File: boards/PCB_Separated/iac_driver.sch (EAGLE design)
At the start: 8 parts, among them IC1 L293D

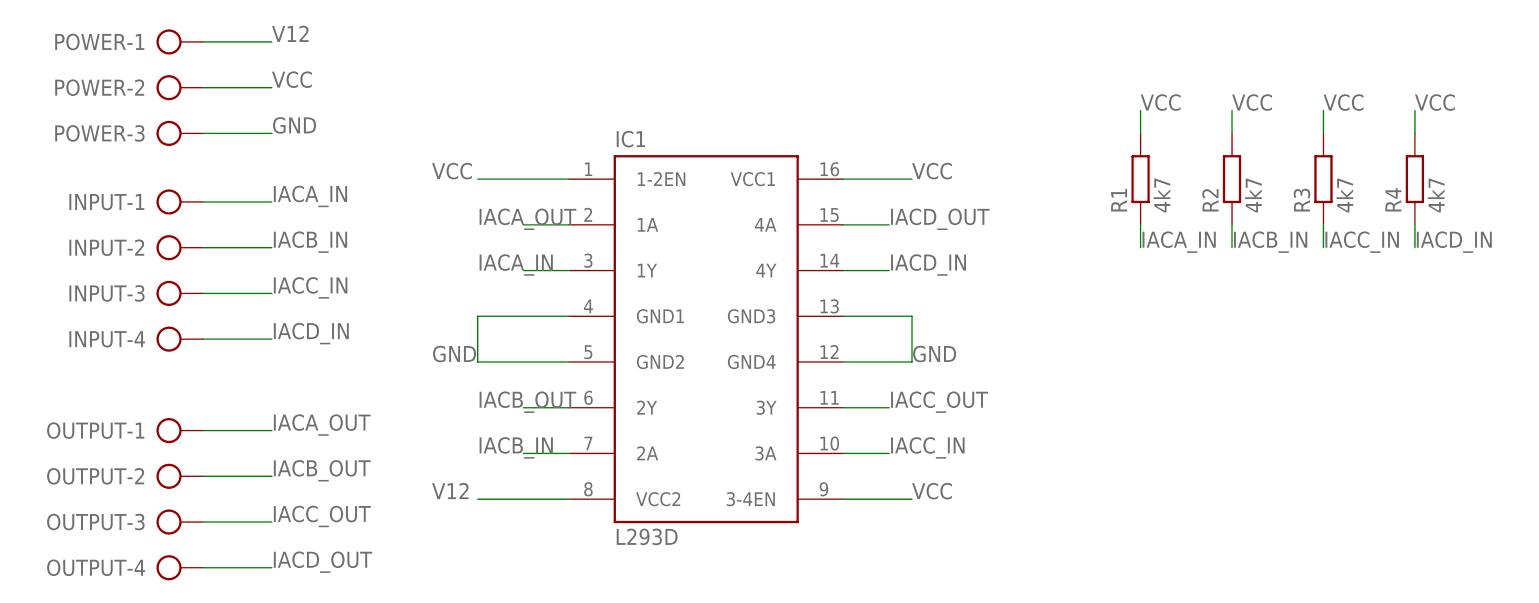
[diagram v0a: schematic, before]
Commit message: IAC progress. Valve already driven, but there a problem with voltage while USB connected to PC
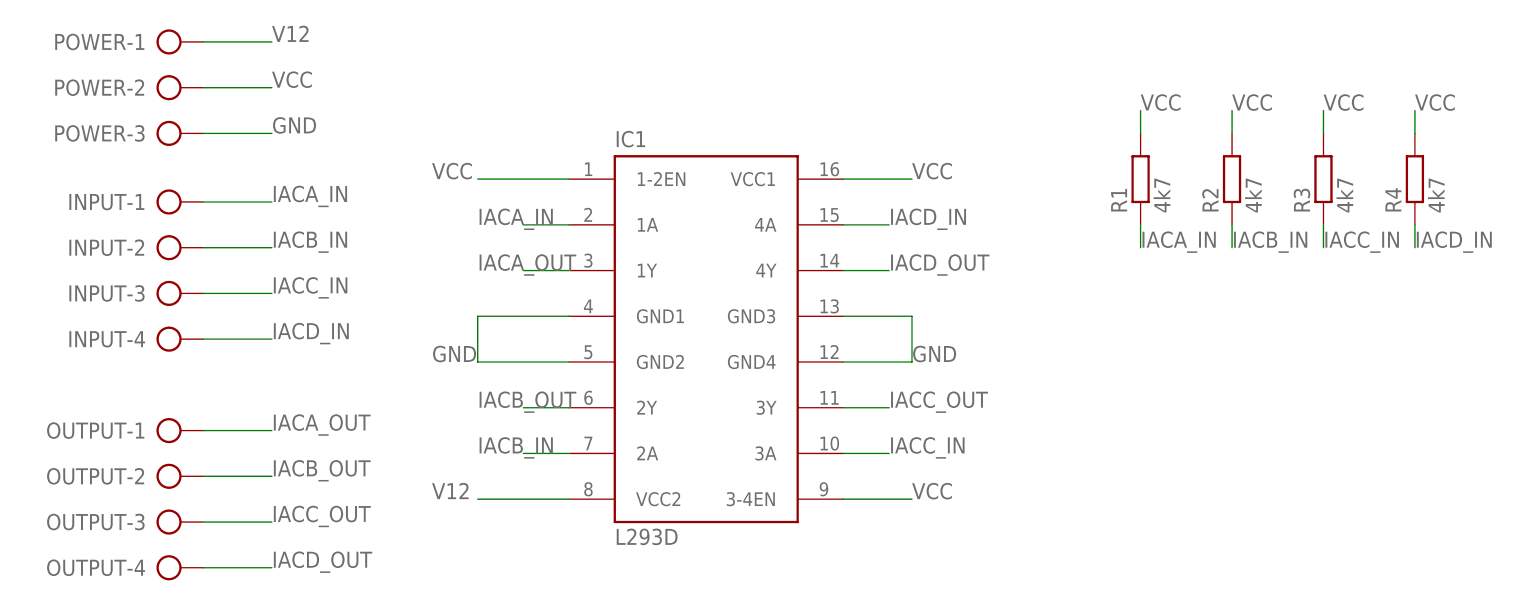
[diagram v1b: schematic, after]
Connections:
- net IACA_IN: now also IC1.1A; no longer IC1.1Y
- net IACA_OUT: now also IC1.1Y; no longer IC1.1A
- net IACD_IN: now also IC1.4A; no longer IC1.4Y
- net IACD_OUT: now also IC1.4Y; no longer IC1.4A
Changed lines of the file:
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@@
 <net name="IACA_OUT" class="0">
-<segment>
-<pinref part="IC1" gate="G$1" pin="1A"/>
-<wire x1="45.72" y1="35.56" x2="40.64" y2="35.56" width="0.1524" layer="91"/>
-<label x="35.56" y="35.56" size="1.778" layer="95"/>
-</segment>
 <segment>
 <pinref part="OUTPUT" gate="-1" pin="KL"/>
@@
 <label x="12.7" y="12.7" size="1.778" layer="95"/>
 </segment>
-</net>
-<net name="IACA_IN" class="0">
 <segment>
 <pinref part="IC1" gate="G$1" pin="1Y"/>
@@
 <label x="35.56" y="30.48" size="1.778" layer="95"/>
 </segment>
+</net>
+<net name="IACA_IN" class="0">
 <segment>
 <pinref part="R1" gate="G$1" pin="1"/>
@@
 <wire x1="5.08" y1="38.1" x2="12.7" y2="38.1" width="0.1524" layer="91"/>
 <label x="12.7" y="38.1" size="1.778" layer="95"/>
+</segment>
+<segment>
+<pinref part="IC1" gate="G$1" pin="1A"/>
+<wire x1="45.72" y1="35.56" x2="40.64" y2="35.56" width="0.1524" layer="91"/>
+<label x="35.56" y="35.56" size="1.778" layer="95"/>
 </segment>
 </net>
@@
 <net name="IACD_OUT" class="0">
 <segment>
-<pinref part="IC1" gate="G$1" pin="4A"/>
-<wire x1="76.2" y1="35.56" x2="81.28" y2="35.56" width="0.1524" layer="91"/>
-<label x="81.28" y="35.56" size="1.778" layer="95"/>
-</segment>
-<segment>
 <pinref part="OUTPUT" gate="-4" pin="KL"/>
 <wire x1="5.08" y1="-2.54" x2="12.7" y2="-2.54" width="0.1524" layer="91"/>
 <label x="12.7" y="-2.54" size="1.778" layer="95"/>
 </segment>
-</net>
-<net name="IACD_IN" class="0">
 <segment>
 <pinref part="IC1" gate="G$1" pin="4Y"/>
@@
 <label x="81.28" y="30.48" size="1.778" layer="95"/>
 </segment>
+</net>
+<net name="IACD_IN" class="0">
 <segment>
 <pinref part="R4" gate="G$1" pin="1"/>
@@
 <label x="12.7" y="22.86" size="1.778" layer="95"/>
 </segment>
+<segment>
+<pinref part="IC1" gate="G$1" pin="4A"/>
+<wire x1="76.2" y1="35.56" x2="81.28" y2="35.56" width="0.1524" layer="91"/>
+<label x="81.28" y="35.56" size="1.778" layer="95"/>
+</segment>
 </net>
